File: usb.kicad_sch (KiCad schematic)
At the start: 11 parts, among them J3 USB_C_Receptacle_USB2.0_16P, U5 USBLC6-2SC6, U8 CP2102N-Axx-xQFN24

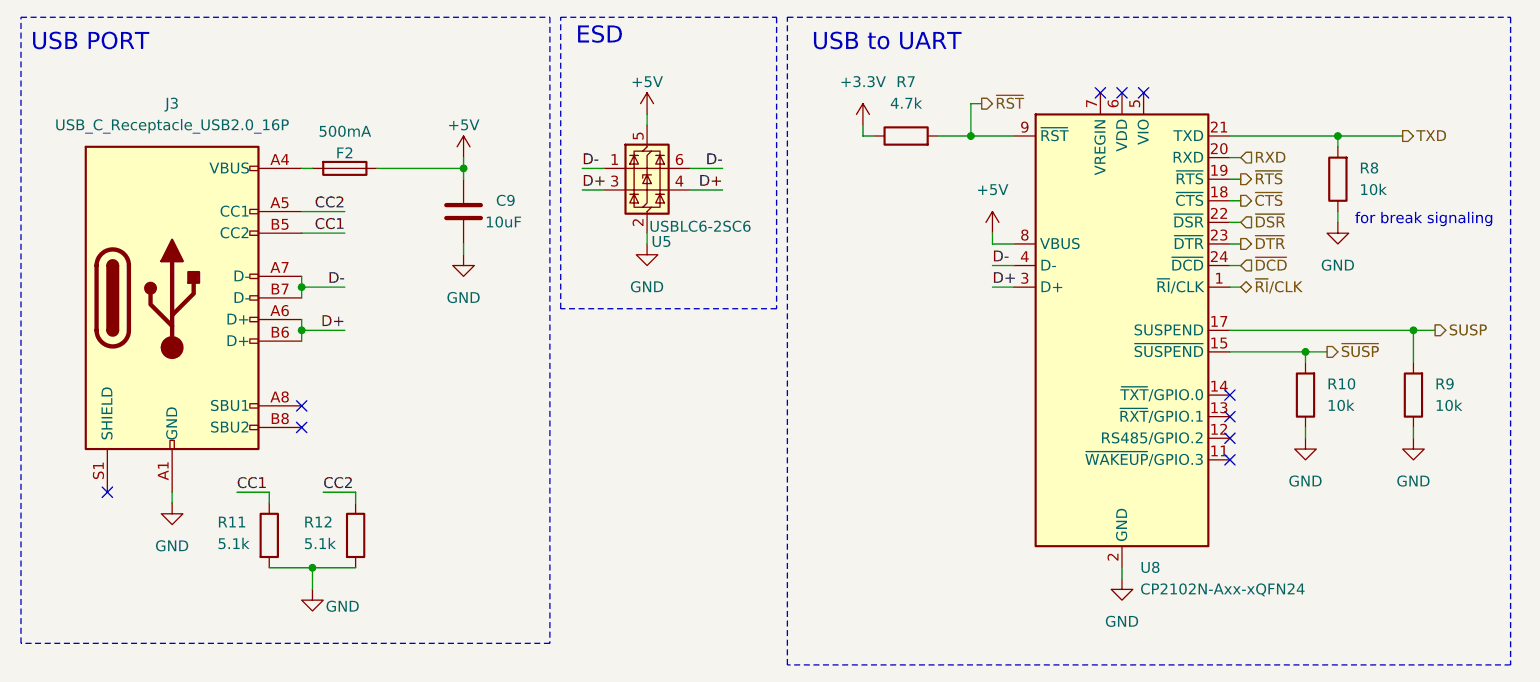
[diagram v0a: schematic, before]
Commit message: reannotated schematic
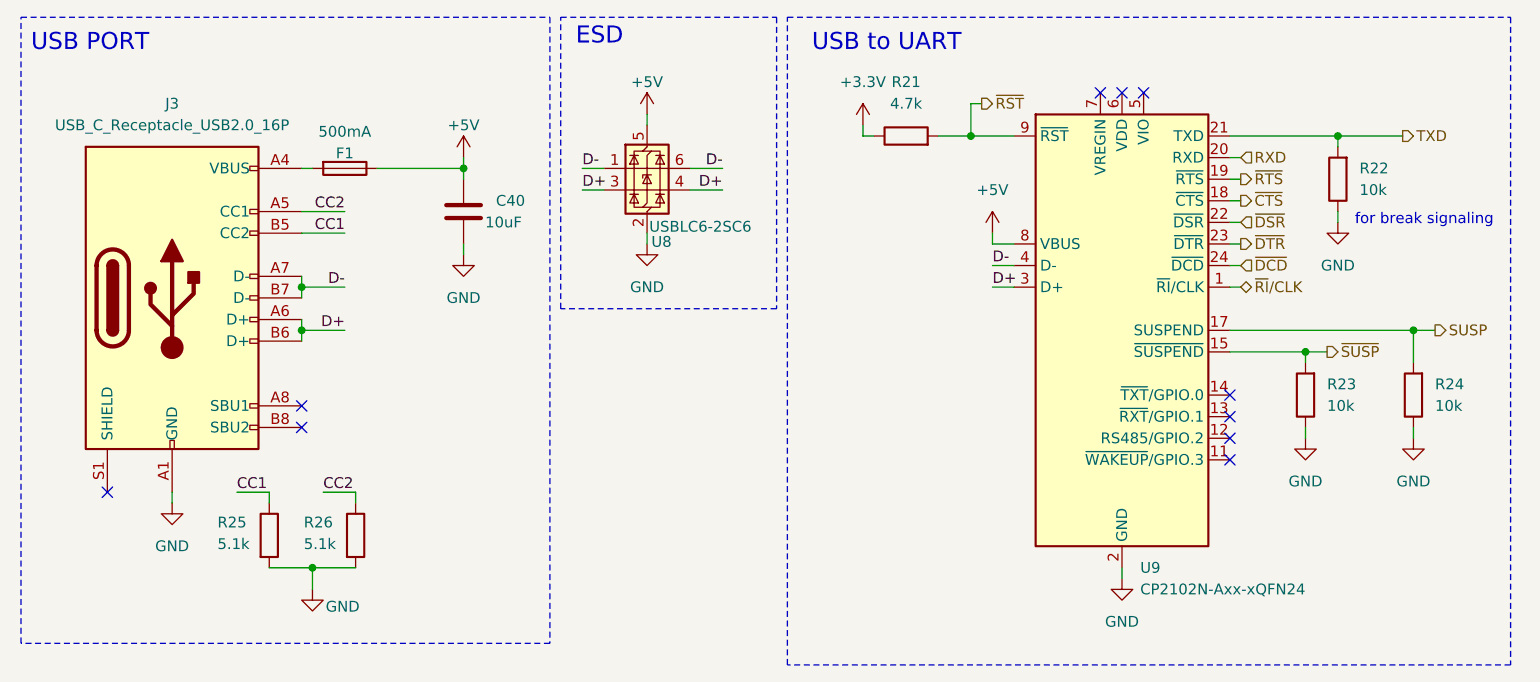
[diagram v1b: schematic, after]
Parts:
- renumbered C9 to C40, F2 to F1, R7 to R21, R8 to R22, R10 to R23, R9 to R24, R11 to R25, R12 to R26, U5 to U8, U8 to U9
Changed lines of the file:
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@@
 		(on_board yes)
 		(dnp no)
-		(property "Reference" "R12"
+		(property "Reference" "R26"
 			(at 45.974 72.136 0)
 			(effects
@@
 			(project "meko-pcb"
 				(path "/bdd43acd-23c1-472b-909a-8e24eb60d56d/f706aad0-fe72-4f1f-8f4a-da2e99c9f80e"
-					(reference "R12")
+					(reference "R26")
 					(unit 1)
 				)
@@
 		(dnp no)
 		(fields_autoplaced yes)
-		(property "Reference" "#PWR013"
+		(property "Reference" "#PWR060"
 			(at 127 41.91 0)
 			(effects
@@
 			(project "meko-pcb"
 				(path "/bdd43acd-23c1-472b-909a-8e24eb60d56d/f706aad0-fe72-4f1f-8f4a-da2e99c9f80e"
-					(reference "#PWR013")
+					(reference "#PWR060")
 					(unit 1)
 				)
@@
 		(dnp no)
 		(fields_autoplaced yes)
-		(property "Reference" "R7"
+		(property "Reference" "R21"
 			(at 116.84 20.32 90)
 			(effects
@@
 			(project ""
 				(path "/bdd43acd-23c1-472b-909a-8e24eb60d56d/f706aad0-fe72-4f1f-8f4a-da2e99c9f80e"
-					(reference "R7")
+					(reference "R21")
 					(unit 1)
 				)
@@
 		(on_board yes)
 		(dnp no)
-		(property "Reference" "R11"
+		(property "Reference" "R25"
 			(at 35.814 72.136 0)
 			(effects
@@
 			(project "meko-pcb"
 				(path "/bdd43acd-23c1-472b-909a-8e24eb60d56d/f706aad0-fe72-4f1f-8f4a-da2e99c9f80e"
-					(reference "R11")
+					(reference "R25")
 					(unit 1)
 				)
@@
 		(dnp no)
 		(fields_autoplaced yes)
-		(property "Reference" "R8"
+		(property "Reference" "R22"
 			(at 170.18 30.4799 0)
 			(effects
@@
 			(project "meko-pcb"
 				(path "/bdd43acd-23c1-472b-909a-8e24eb60d56d/f706aad0-fe72-4f1f-8f4a-da2e99c9f80e"
-					(reference "R8")
+					(reference "R22")
 					(unit 1)
 				)
@@
 		(dnp no)
 		(fields_autoplaced yes)
-		(property "Reference" "#PWR074"
+		(property "Reference" "#PWR062"
 			(at 64.77 46.99 0)
 			(effects
@@
 			(project "meko-pcb"
 				(path "/bdd43acd-23c1-472b-909a-8e24eb60d56d/f706aad0-fe72-4f1f-8f4a-da2e99c9f80e"
-					(reference "#PWR074")
+					(reference "#PWR062")
 					(unit 1)
 				)
@@
 		(dnp no)
 		(fields_autoplaced yes)
-		(property "Reference" "#PWR017"
+		(property "Reference" "#PWR059"
 			(at 167.64 43.18 0)
 			(effects
@@
 			(project "meko-pcb"
 				(path "/bdd43acd-23c1-472b-909a-8e24eb60d56d/f706aad0-fe72-4f1f-8f4a-da2e99c9f80e"
-					(reference "#PWR017")
+					(reference "#PWR059")
 					(unit 1)
 				)
@@
 		(dnp no)
 		(fields_autoplaced yes)
-		(property "Reference" "R10"
+		(property "Reference" "R23"
 			(at 166.37 55.8799 0)
 			(effects
@@
 			(project "meko-pcb"
 				(path "/bdd43acd-23c1-472b-909a-8e24eb60d56d/f706aad0-fe72-4f1f-8f4a-da2e99c9f80e"
-					(reference "R10")
+					(reference "R23")
 					(unit 1)
 				)
@@
 		(on_board yes)
 		(dnp no)
-		(property "Reference" "#PWR09"
+		(property "Reference" "#PWR067"
 			(at 46.99 86.36 0)
 			(effects
@@
 			(project "meko-pcb"
 				(path "/bdd43acd-23c1-472b-909a-8e24eb60d56d/f706aad0-fe72-4f1f-8f4a-da2e99c9f80e"
-					(reference "#PWR09")
+					(reference "#PWR067")
 					(unit 1)
 				)
@@
 		(dnp no)
 		(fields_autoplaced yes)
-		(property "Reference" "#PWR020"
+		(property "Reference" "#PWR063"
 			(at 163.83 68.58 0)
 			(effects
@@
 			(project "meko-pcb"
 				(path "/bdd43acd-23c1-472b-909a-8e24eb60d56d/f706aad0-fe72-4f1f-8f4a-da2e99c9f80e"
-					(reference "#PWR020")
+					(reference "#PWR063")
 					(unit 1)
 				)
@@
 		(on_board yes)
 		(dnp no)
-		(property "Reference" "F2"
+		(property "Reference" "F1"
 			(at 50.8 28.702 90)
 			(effects
@@
 			(project "meko-pcb"
 				(path "/bdd43acd-23c1-472b-909a-8e24eb60d56d/f706aad0-fe72-4f1f-8f4a-da2e99c9f80e"
-					(reference "F2")
+					(reference "F1")
 					(unit 1)
 				)
@@
 		(dnp no)
 		(fields_autoplaced yes)
-		(property "Reference" "#PWR010"
+		(property "Reference" "#PWR061"
 			(at 86.36 45.72 0)
 			(effects
@@
 			(project "meko-pcb"
 				(path "/bdd43acd-23c1-472b-909a-8e24eb60d56d/f706aad0-fe72-4f1f-8f4a-da2e99c9f80e"
-					(reference "#PWR010")
+					(reference "#PWR061")
 					(unit 1)
 				)
@@
 		(on_board yes)
 		(dnp no)
-		(property "Reference" "C9"
+		(property "Reference" "C40"
 			(at 68.58 34.2899 0)
 			(effects
@@
 			(project "meko-pcb"
 				(path "/bdd43acd-23c1-472b-909a-8e24eb60d56d/f706aad0-fe72-4f1f-8f4a-da2e99c9f80e"
-					(reference "C9")
+					(reference "C40")
 					(unit 1)
 				)
@@
 		(dnp no)
 		(fields_autoplaced yes)
-		(property "Reference" "#PWR015"
+		(property "Reference" "#PWR057"
 			(at 111.76 29.21 0)
 			(effects
@@
 			(project ""
 				(path "/bdd43acd-23c1-472b-909a-8e24eb60d56d/f706aad0-fe72-4f1f-8f4a-da2e99c9f80e"
-					(reference "#PWR015")
+					(reference "#PWR057")
 					(unit 1)
 				)
@@
 		(dnp no)
 		(fields_autoplaced yes)
-		(property "Reference" "U8"
+		(property "Reference" "U9"
 			(at 144.3833 77.47 0)
 			(effects
@@
 			(project ""
 				(path "/bdd43acd-23c1-472b-909a-8e24eb60d56d/f706aad0-fe72-4f1f-8f4a-da2e99c9f80e"
-					(reference "U8")
+					(reference "U9")
 					(unit 1)
 				)
@@
 		(on_board yes)
 		(dnp no)
-		(property "Reference" "#PWR012"
+		(property "Reference" "#PWR056"
 			(at 86.36 27.94 0)
 			(effects
@@
 			(project "meko-pcb"
 				(path "/bdd43acd-23c1-472b-909a-8e24eb60d56d/f706aad0-fe72-4f1f-8f4a-da2e99c9f80e"
-					(reference "#PWR012")
+					(reference "#PWR056")
 					(unit 1)
 				)
@@
 		(on_board yes)
 		(dnp no)
-		(property "Reference" "U5"
+		(property "Reference" "U8"
 			(at 86.868 39.116 0)
 			(effects
@@
 			(project "meko-pcb"
 				(path "/bdd43acd-23c1-472b-909a-8e24eb60d56d/f706aad0-fe72-4f1f-8f4a-da2e99c9f80e"
-					(reference "U5")
+					(reference "U8")
 					(unit 1)
 				)
@@
 		(dnp no)
 		(fields_autoplaced yes)
-		(property "Reference" "#PWR014"
+		(property "Reference" "#PWR066"
 			(at 142.24 85.09 0)
 			(effects
@@
 			(project "meko-pcb"
 				(path "/bdd43acd-23c1-472b-909a-8e24eb60d56d/f706aad0-fe72-4f1f-8f4a-da2e99c9f80e"
-					(reference "#PWR014")
+					(reference "#PWR066")
 					(unit 1)
 				)
@@
 		(dnp no)
 		(fields_autoplaced yes)
-		(property "Reference" "#PWR018"
+		(property "Reference" "#PWR064"
 			(at 176.53 68.58 0)
 			(effects
@@
 			(project "meko-pcb"
 				(path "/bdd43acd-23c1-472b-909a-8e24eb60d56d/f706aad0-fe72-4f1f-8f4a-da2e99c9f80e"
-					(reference "#PWR018")
+					(reference "#PWR064")
 					(unit 1)
 				)
@@
 		(dnp no)
 		(fields_autoplaced yes)
-		(property "Reference" "#PWR08"
+		(property "Reference" "#PWR065"
 			(at 30.48 76.2 0)
 			(effects
@@
 			(project ""
 				(path "/bdd43acd-23c1-472b-909a-8e24eb60d56d/f706aad0-fe72-4f1f-8f4a-da2e99c9f80e"
-					(reference "#PWR08")
+					(reference "#PWR065")
 					(unit 1)
 				)
@@
 		(dnp no)
 		(fields_autoplaced yes)
-		(property "Reference" "R9"
+		(property "Reference" "R24"
 			(at 179.07 55.8799 0)
 			(effects
@@
 			(project "meko-pcb"
 				(path "/bdd43acd-23c1-472b-909a-8e24eb60d56d/f706aad0-fe72-4f1f-8f4a-da2e99c9f80e"
-					(reference "R9")
+					(reference "R24")
 					(unit 1)
 				)
@@
 		(on_board yes)
 		(dnp no)
-		(property "Reference" "#PWR011"
+		(property "Reference" "#PWR058"
 			(at 64.77 33.02 0)
 			(effects
@@
 			(project "meko-pcb"
 				(path "/bdd43acd-23c1-472b-909a-8e24eb60d56d/f706aad0-fe72-4f1f-8f4a-da2e99c9f80e"
-					(reference "#PWR011")
-					(unit 1)
-				)
+					(reference "#PWR058")
+					(unit 1)
+				)

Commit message: added titles to sheets
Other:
- title: (none) -> USB
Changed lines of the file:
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@@
 	(generator_version "9.0")
 	(paper "A5")
+	(title_block
+		(title "USB")
+	)
 	(rectangle
 		(start 12.7 12.7)

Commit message: small fixes
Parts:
- R21: value 4.7k -> 10k
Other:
- moved on the sheet: R21
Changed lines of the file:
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@@
 	)
 	(junction
-		(at 124.46 26.67)
+		(at 128.27 26.67)
 		(diameter 0)
 		(color 0 0 0 0)
@@
 	(wire
 		(pts
-			(xy 124.46 22.86) (xy 125.73 22.86)
+			(xy 128.27 26.67) (xy 127 26.67)
 		)
 		(stroke
@@
 	(wire
 		(pts
-			(xy 111.76 26.67) (xy 113.03 26.67)
-		)
-		(stroke
-			(width 0)
-			(type default)
-		)
-	)
-	(wire
-		(pts
 			(xy 78.74 33.02) (xy 81.28 33.02)
 		)
@@
 	(wire
 		(pts
-			(xy 124.46 26.67) (xy 129.54 26.67)
-		)
-		(stroke
-			(width 0)
-			(type default)
-		)
-	)
-	(wire
-		(pts
 			(xy 127 39.37) (xy 129.54 39.37)
 		)
@@
 	(wire
 		(pts
-			(xy 124.46 22.86) (xy 124.46 26.67)
-		)
-		(stroke
-			(width 0)
-			(type default)
-		)
-	)
-	(wire
-		(pts
 			(xy 86.36 39.37) (xy 86.36 38.1)
 		)
@@
 	(wire
 		(pts
-			(xy 120.65 26.67) (xy 124.46 26.67)
-		)
-		(stroke
-			(width 0)
-			(type default)
-		)
-	)
-	(wire
-		(pts
 			(xy 78.74 30.48) (xy 81.28 30.48)
 		)
@@
 	(wire
 		(pts
+			(xy 128.27 25.4) (xy 128.27 26.67)
+		)
+		(stroke
+			(width 0)
+			(type default)
+		)
+	)
+	(wire
+		(pts
+			(xy 128.27 26.67) (xy 129.54 26.67)
+		)
+		(stroke
+			(width 0)
+			(type default)
+		)
+	)
+	(wire
+		(pts
 			(xy 45.72 44.45) (xy 50.8 44.45)
 		)
@@
 	(wire
 		(pts
-			(xy 111.76 25.4) (xy 111.76 26.67)
+			(xy 128.27 16.51) (xy 128.27 17.78)
 		)
 		(stroke
@@
 	(hierarchical_label "~{RST}"
 		(shape output)
-		(at 125.73 22.86 0)
-		(effects
-			(font
-				(size 1.27 1.27)
-			)
-			(justify left)
+		(at 127 26.67 180)
+		(effects
+			(font
+				(size 1.27 1.27)
+			)
+			(justify right)
 		)
 	)
@@
 	(symbol
 		(lib_id "Device:R")
-		(at 116.84 26.67 90)
+		(at 128.27 21.59 0)
 		(unit 1)
 		(exclude_from_sim no)
@@
 		(fields_autoplaced yes)
 		(property "Reference" "R21"
-			(at 116.84 20.32 90)
-			(effects
-				(font
-					(size 1.27 1.27)
-				)
-			)
-		)
-		(property "Value" "4.7k"
-			(at 116.84 22.86 90)
-			(effects
-				(font
-					(size 1.27 1.27)
-				)
+			(at 130.81 20.3199 0)
+			(effects
+				(font
+					(size 1.27 1.27)
+				)
+				(justify left)
+			)
+		)
+		(property "Value" "10k"
+			(at 130.81 22.8599 0)
+			(effects
+				(font
+					(size 1.27 1.27)
+				)
+				(justify left)
 			)
 		)
 		(property "Footprint" ""
-			(at 116.84 28.448 90)
+			(at 126.492 21.59 90)
 			(effects
 				(font
@@
 		)
 		(property "Datasheet" "~"
-			(at 116.84 26.67 0)
+			(at 128.27 21.59 0)
 			(effects
 				(font
@@
 		)
 		(property "Description" "Resistor"
-			(at 116.84 26.67 0)
+			(at 128.27 21.59 0)
 			(effects
 				(font
@@
 	(symbol
 		(lib_id "power:+3.3V")
-		(at 111.76 25.4 0)
+		(at 128.27 16.51 0)
 		(unit 1)
 		(exclude_from_sim no)
@@
 		(on_board yes)
 		(dnp no)
-		(fields_autoplaced yes)
 		(property "Reference" "#PWR057"
-			(at 111.76 29.21 0)
+			(at 128.27 20.32 0)
 			(effects
 				(font
@@
 		)
 		(property "Value" "+3.3V"
-			(at 111.76 20.32 0)
+			(at 131.826 14.986 0)
 			(effects
 				(font
@@
 		)
 		(property "Footprint" ""
-			(at 111.76 25.4 0)
+			(at 128.27 16.51 0)
 			(effects
 				(font
@@
 		)
 		(property "Datasheet" ""
-			(at 111.76 25.4 0)
+			(at 128.27 16.51 0)
 			(effects
 				(font
@@
 		)
 		(property "Description" "Power symbol creates a global label with name \"+3.3V\""
-			(at 111.76 25.4 0)
-			(effects
-				(font
+			(at 128.27 16.51 0)
+			(effects
+				(font

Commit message: fuel gauge ic
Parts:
- C40: footprint (none) -> Capacitor_SMD:C_0402_1005Metric
- R21, R22, R23, R24: footprint (none) -> Resistor_SMD:R_0402_1005Metric
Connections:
- net +3.3V renamed +3V3
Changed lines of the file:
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@@
+	)
+	(symbol
+		(lib_id "power:+3V3")
+		(at 128.27 16.51 0)
+		(unit 1)
+		(exclude_from_sim no)
+		(in_bom yes)
+		(on_board yes)
+		(dnp no)
+		(property "Reference" "#PWR057"
+			(at 128.27 20.32 0)
+			(effects
+				(font
+					(size 1.27 1.27)
+				)
+				(hide yes)
+			)
+		)
+		(property "Value" "+3V3"
+			(at 131.826 14.986 0)
+			(effects
+				(font
+					(size 1.27 1.27)
+				)
+			)
+		)
+		(property "Footprint" ""
+			(at 128.27 16.51 0)
+			(effects
+				(font
+					(size 1.27 1.27)
+				)
+				(hide yes)
+			)
+		)
+		(property "Datasheet" ""
+			(at 128.27 16.51 0)
+			(effects
+				(font
+					(size 1.27 1.27)
+				)
+				(hide yes)
+			)
+		)
+		(property "Description" "Power symbol creates a global label with name \"+3V3\""
+			(at 128.27 16.51 0)
+			(effects
+				(font
+					(size 1.27 1.27)
+				)
+				(hide yes)
+			)
+		)
+		(pin "1"
+		)
+		(instances
+			(project "meko-pcb"
+				(path "/bdd43acd-23c1-472b-909a-8e24eb60d56d/f706aad0-fe72-4f1f-8f4a-da2e99c9f80e"
+					(reference "#PWR057")
+					(unit 1)
+				)
+			)
+		)
 	)
 	(symbol
@@
 			)
 		)
-		(property "Footprint" ""
+		(property "Footprint" "Resistor_SMD:R_0402_1005Metric"
 			(at 126.492 21.59 90)
 			(effects
@@
 			)
 		)
-		(property "Footprint" ""
+		(property "Footprint" "Resistor_SMD:R_0402_1005Metric"
 			(at 169.418 31.75 90)
 			(effects
@@
 			)
 		)
-		(property "Footprint" ""
+		(property "Footprint" "Resistor_SMD:R_0402_1005Metric"
 			(at 165.608 57.15 90)
 			(effects
@@
 			)
 		)
-		(property "Footprint" ""
+		(property "Footprint" "Capacitor_SMD:C_0402_1005Metric"
 			(at 65.7352 39.37 0)
 			(effects
@@
 				(path "/bdd43acd-23c1-472b-909a-8e24eb60d56d/f706aad0-fe72-4f1f-8f4a-da2e99c9f80e"
 					(reference "C40")
-					(unit 1)
-				)
-			)
-		)
-	)
-	(symbol
-		(lib_id "power:+3.3V")
-		(at 128.27 16.51 0)
-		(unit 1)
-		(exclude_from_sim no)
-		(in_bom yes)
-		(on_board yes)
-		(dnp no)
-		(property "Reference" "#PWR057"
-			(at 128.27 20.32 0)
-			(effects
-				(font
-					(size 1.27 1.27)
-				)
-				(hide yes)
-			)
-		)
-		(property "Value" "+3.3V"
-			(at 131.826 14.986 0)
-			(effects
-				(font
-					(size 1.27 1.27)
-				)
-			)
-		)
-		(property "Footprint" ""
-			(at 128.27 16.51 0)
-			(effects
-				(font
-					(size 1.27 1.27)
-				)
-				(hide yes)
-			)
-		)
-		(property "Datasheet" ""
-			(at 128.27 16.51 0)
-			(effects
-				(font
-					(size 1.27 1.27)
-				)
-				(hide yes)
-			)
-		)
-		(property "Description" "Power symbol creates a global label with name \"+3.3V\""
-			(at 128.27 16.51 0)
-			(effects
-				(font
-					(size 1.27 1.27)
-				)
-				(hide yes)
-			)
-		)
-		(pin "1"
-		)
-		(instances
-			(project ""
-				(path "/bdd43acd-23c1-472b-909a-8e24eb60d56d/f706aad0-fe72-4f1f-8f4a-da2e99c9f80e"
-					(reference "#PWR057")
 					(unit 1)
 				)
@@
 			)
 		)
-		(property "Footprint" ""
+		(property "Footprint" "Resistor_SMD:R_0402_1005Metric"
 			(at 178.308 57.15 90)
 			(effects

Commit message: layout
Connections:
- net GND: now also J3.S1 (SHIELD)
- no-connect marks 10 -> 9
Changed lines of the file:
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@@
+	)
+	(junction
+		(at 30.48 69.85)
+		(diameter 0)
+		(color 0 0 0 0)
 	)
 	(junction
@@
 	)
 	(no_connect
-		(at 22.86 68.58)
-	)
-	(no_connect
 		(at 154.94 62.23)
 	)
@@
 	(wire
 		(pts
+			(xy 30.48 69.85) (xy 30.48 68.58)
+		)
+		(stroke
+			(width 0)
+			(type default)
+		)
+	)
+	(wire
+		(pts
 			(xy 156.21 41.91) (xy 154.94 41.91)
 		)
@@
 	(wire
 		(pts
-			(xy 30.48 69.85) (xy 30.48 68.58)
+			(xy 22.86 69.85) (xy 22.86 68.58)
 		)
 		(stroke
@@
 		)
 		(stroke
+			(width 0)
+			(type default)
+		)
+	)
+	(wire
+		(pts
+			(xy 22.86 69.85) (xy 30.48 69.85)
+		)
+		(stroke
